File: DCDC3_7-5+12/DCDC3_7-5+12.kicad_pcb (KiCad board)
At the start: 2 copper layers, 63.5 x 75.8 mm, 29 parts, among them IC1 TPS61088QRHLRQ1, J1 FAN, T1 + 3.7V -, T2 + 12V -, T3 + 5V -, U2 XL6009

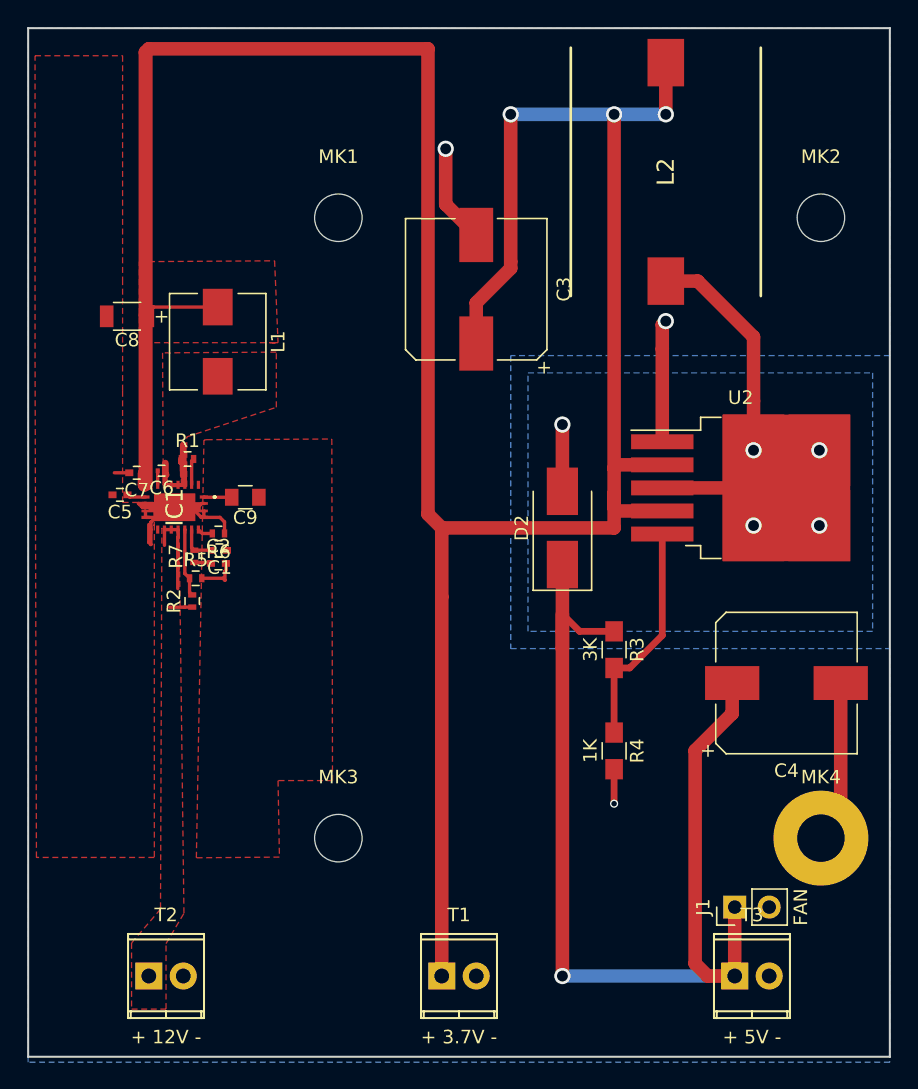
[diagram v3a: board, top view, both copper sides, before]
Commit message: Final version of aux 5v and 12v power supply.
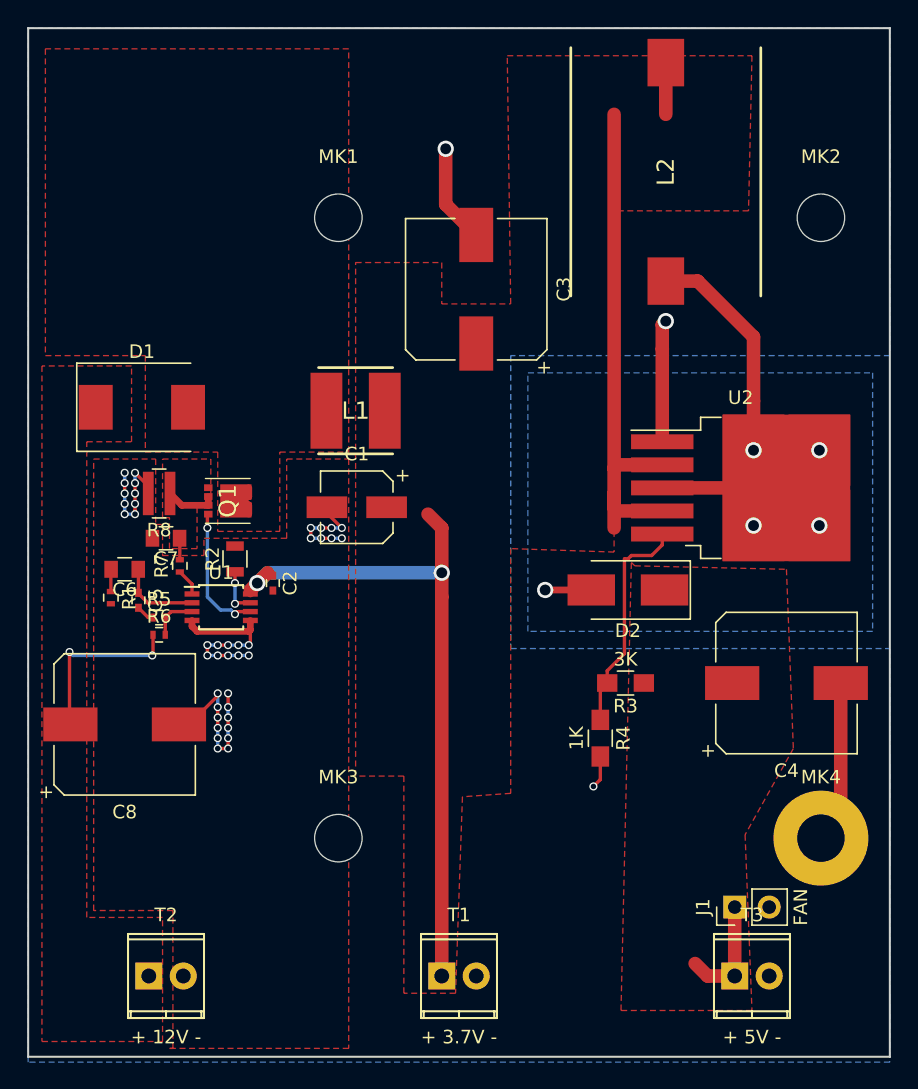
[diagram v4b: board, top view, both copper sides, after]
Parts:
- removed C9: 3.3uf, Capacitors_SMD:C_0805
- removed IC1: TPS61088QRHLRQ1, TPS61088QRHLRQ1:TPS61088QRHLRQ1
- added D1: 550mV, Diodes_SMD:D_SMC, F.Cu at (110.0, 91.4)
- added Q1: CSD16323Q3, Q3:Q3, F.Cu at (116.3, 98.3)
- added R8: 5m, Resistors_SMD:R_0612, F.Cu at (111.3, 97.8)
- added U1: LM3488, Housings_SSOP:TSSOP-8_3x3mm_Pitch0.65mm, F.Cu at (115.8, 106.2)
- C1: value C_Small -> 220uf; footprint Capacitors_SMD:C_0402 -> Capacitors_SMD:CP_Elec_5x5.7
- C2: value C_Small -> 100nf
- C5: value 47nf -> 1nf
- C6: value .1uf -> 15nf; footprint Capacitors_SMD:C_0201 -> Capacitors_SMD:C_0805
- C7: value .1uf -> 10pf; footprint Capacitors_SMD:C_0402 -> Capacitors_SMD:C_0805
- C8: value 10uf -> 560uF; footprint MyCaps:C_1206_Pol -> Capacitors_SMD:CP_Elec_10x10.5
- L1: value 1.5uh -> 1.8uh; footprint Inductors_SMD:L_Wuerth_HCI-7040 -> XAL6030:INDM5564X32N
- R1: value 290K -> 6.81K
- R2: value 500K -> 40K; footprint Resistors_SMD:R_0402 -> Resistors_SMD:R_0805
- R5: value 56K -> 1K
- R6: value 49.9K -> 8.45K
- R7: value R -> 100
- moved C8 30.1 mm to (108.7, 114.8), turned to 0 degrees
- moved R1 11.7 mm to (107.7, 105.5), turned to 270 degrees
- moved L1 11.4 mm to (125.7, 91.7), turned to 180 degrees
- moved C1 10.6 mm to (125.8, 98.8)
- moved R6 8.65 mm to (111.3, 108.2), turned to 0 degrees
- moved C5 7.89 mm to (109.7, 105.7), turned to 270 degrees
- moved C6 7.76 mm to (108.7, 103.4)
- moved D2 6.65 mm to (145.8, 104.9), turned to 180 degrees
- moved C7 5.29 mm to (111.8, 101.1)
- moved R2 4.42 mm to (116.8, 102.6)
- moved C2 4.27 mm to (119.6, 104.4), turned to 270 degrees
- moved R5 3.95 mm to (111.3, 106.9)
- moved R3 2.60 mm to (145.6, 111.8), turned to 180 degrees
- moved R4 1.38 mm to (143.8, 115.8)
- moved R7 1.28 mm to (112.8, 103.1)
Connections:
- C1 pad 1: GND -> /DCDC 3.7 - 12/3.7V
- C1 pad 2: Net-(C1-Pad2) -> GND
- C2 pad 1: Net-(C2-Pad1) -> /DCDC 3.7 - 12/3.7V
- C6 pad 1: Net-(C6-Pad1) -> Net-(C5-Pad1)
- C7 pad 1: /DCDC 3.7 - 12/3.7V -> Net-(C7-Pad1)
- C8 pad 1: /DCDC 3.7 - 12/3.7V -> /DCDC 3.7 - 12/12V
- L1 pad 2: Net-(C6-Pad1) -> Net-(D1-Pad2)
- R1 pad 1: Net-(C6-Pad1) -> Net-(C6-Pad2)
- R1 pad 2: Net-(IC1-Pad3) -> GND
- R2 pad 1: /DCDC 3.7 - 12/12V -> Net-(R2-Pad1)
- R2 pad 2: Net-(IC1-Pad17) -> GND
- R5 pad 1: Net-(IC1-Pad17) -> GND
- R5 pad 2: GND -> Net-(R5-Pad2)
- R6 pad 1: GND -> /DCDC 3.7 - 12/12V
- R6 pad 2: Net-(IC1-Pad19) -> Net-(R5-Pad2)
- R7 pad 1: Net-(C2-Pad1) -> Net-(R7-Pad1)
- R7 pad 2: Net-(C1-Pad2) -> Net-(C7-Pad1)
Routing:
- net /DCDC 3.7 - 12/3.7V: track 244.9 -> 93.6 mm, vias 3 -> 2
- net /DCDC 3.7 to 5/5V: track 80.1 -> 8.38 mm, vias 1 -> 0
- net Net-(C6-Pad1): track 14.2 -> 0.00 mm
- net GND: track 63.7 -> 75.9 mm, vias 3 -> 43
- net Net-(Q1-Pad4): track 0.00 -> 9.89 mm, vias 0 -> 2
- net Net-(C7-Pad1): track 0.00 -> 5.42 mm
- net Net-(IC1-Pad17): track 5.05 -> 0.00 mm
- net /DCDC 3.7 - 12/12V: track 8.40 -> 13.1 mm, vias 0 -> 2
- net Net-(C5-Pad1): track 1.40 -> 6.02 mm
- net Net-(D1-Pad2): track 0.00 -> 4.24 mm
- net Net-(R2-Pad1): track 0.00 -> 3.52 mm, vias 0 -> 2
- net Net-(R5-Pad2): track 0.00 -> 3.42 mm
- net Net-(C1-Pad2): track 2.91 -> 0.00 mm
- net Net-(C9-Pad2): track 2.06 -> 0.00 mm
- net Net-(R7-Pad1): track 0.00 -> 1.99 mm
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- added copper zone on F.Cu, net /DCDC 3.7 to 5/5V
- added copper zone on F.Cu, net Net-(C7-Pad1)
- added copper zone on F.Cu, net Net-(D1-Pad2)
- removed copper zone on F.Cu, net Net-(C6-Pad1)
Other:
- rule via_min_drill: 0.3 -> 0.1
- rule via_min_size: 0.4 -> 0.3

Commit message: Final version of aux 5v and 12v power supply.
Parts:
- added fd1: Fiducial_classic_Small_SilkscreenTop_Type1, Fiducials:Fiducial_classic_Small_SilkscreenTop_Type1, F.Cu at (148.6, 122.9)
- added fd2: Fiducial_classic_Small_SilkscreenTop_Type1, Fiducials:Fiducial_classic_Small_SilkscreenTop_Type1, F.Cu at (137.7, 95.0)
- added fd3: Fiducial_classic_Small_SilkscreenTop_Type1, Fiducials:Fiducial_classic_Small_SilkscreenTop_Type1, F.Cu at (110.0, 72.4)
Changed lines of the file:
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@@
 (kicad_pcb (version 4) (host pcbnew 4.0.7+dfsg1-1ubuntu2)
   (general
-    (links 62)
+    (links 0)
     (no_connects 0)
-    (area 101.524999 54.45 183.11 139.700001)
+    (area 101.524999 63.424999 165.175001 139.375001)
     (thickness 1.6)
     (drawings 12)
     (tracks 204)
     (zones 0)
-    (modules 31)
+    (modules 34)
     (nets 15)
   )
@@
     (visible_elements FFFFFF7F)
     (pcbplotparams
-      (layerselection 0x00030_80000001)
-      (usegerberextensions false)
+      (layerselection 0x3ffff_80000001)
+      (usegerberextensions true)
       (excludeedgelayer true)
       (linewidth 0.100000)
-      (plotframeref false)
+      (plotframeref true)
       (viasonmask false)
       (mode 1)
@@
       (outputformat 1)
       (mirror false)
-      (drillshape 1)
+      (drillshape 0)
       (scaleselection 1)
-      (outputdirectory ""))
+      (outputdirectory Gerber))
   )
   (net 0 "")
@@
     )
   )
+  (module Fiducials:Fiducial_classic_Small_SilkscreenTop_Type1 (layer F.Cu)
+    (at 109.982 72.39)
+    (descr "Fiducial, Classical, Small, Copper Top, Typ 1, Passermarke,")
+    (tags "Fiducial, Classical, Small, Copper Top, Typ 1, Passermarke,")
+    (fp_text reference fd3 (at 0 -3.556) (layer F.SilkS)
+      (effects (font (size 1 1) (thickness 0.15)))
+    )
+    (fp_text value Fiducial_classic_Small_SilkscreenTop_Type1 (at 0.34036 3.4798) (layer F.Fab) hide
+      (effects (font (size 1 1) (thickness 0.15)))
+    )
+    (fp_line (start -1.50114 0) (end 1.50114 0) (layer F.SilkS) (width 0.15))
+    (fp_line (start 0 -1.50114) (end 0 1.50114) (layer F.SilkS) (width 0.15))
+    (fp_circle (center 0 0) (end 1.50114 0) (layer F.SilkS) (width 0.15))
+    (pad ~ smd circle (at 0 0) (size 4.50088 4.50088) (layers F.Mask)
+      (solder_mask_margin 2.99974))
+  )
+  (module Fiducials:Fiducial_classic_Small_SilkscreenTop_Type1 (layer F.Cu)
+    (at 148.59 122.936)
+    (descr "Fiducial, Classical, Small, Copper Top, Typ 1, Passermarke,")
+    (tags "Fiducial, Classical, Small, Copper Top, Typ 1, Passermarke,")
+    (fp_text reference fd1 (at 0 -3.556) (layer F.SilkS)
+      (effects (font (size 1 1) (thickness 0.15)))
+    )
+    (fp_text value Fiducial_classic_Small_SilkscreenTop_Type1 (at 0.34036 3.4798) (layer F.Fab) hide
+      (effects (font (size 1 1) (thickness 0.15)))
+    )
+    (fp_line (start -1.50114 0) (end 1.50114 0) (layer F.SilkS) (width 0.15))
+    (fp_line (start 0 -1.50114) (end 0 1.50114) (layer F.SilkS) (width 0.15))
+    (fp_circle (center 0 0) (end 1.50114 0) (layer F.SilkS) (width 0.15))
+    (pad ~ smd circle (at 0 0) (size 4.50088 4.50088) (layers F.Mask)
+      (solder_mask_margin 2.99974))
+  )
+  (module Fiducials:Fiducial_classic_Small_SilkscreenTop_Type1 (layer F.Cu)
+    (at 137.668 94.996)
+    (descr "Fiducial, Classical, Small, Copper Top, Typ 1, Passermarke,")
+    (tags "Fiducial, Classical, Small, Copper Top, Typ 1, Passermarke,")
+    (fp_text reference fd2 (at 0 -3.556) (layer F.SilkS)
+      (effects (font (size 1 1) (thickness 0.15)))
+    )
+    (fp_text value Fiducial_classic_Small_SilkscreenTop_Type1 (at 0.34036 3.4798) (layer F.Fab) hide
+      (effects (font (size 1 1) (thickness 0.15)))
+    )
+    (fp_line (start -1.50114 0) (end 1.50114 0) (layer F.SilkS) (width 0.15))
+    (fp_line (start 0 -1.50114) (end 0 1.50114) (layer F.SilkS) (width 0.15))
+    (fp_circle (center 0 0) (end 1.50114 0) (layer F.SilkS) (width 0.15))
+    (pad ~ smd circle (at 0 0) (size 4.50088 4.50088) (layers F.Mask)
+      (solder_mask_margin 2.99974))
+  )
   (gr_line (start 160.02 77.47) (end 124.46 77.47) (layer Dwgs.User) (width 0.2))
